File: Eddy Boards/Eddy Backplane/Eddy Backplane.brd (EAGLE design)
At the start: 154.2 x 120.7 mm, 87 parts, among them J1 USB_MINI-B_SMT, P1 39-30-02?_S, P2 RB1-125BAG1A, P3 39-30-04?_S, Q1 310mA/60V/1.6Ω, Q2 310mA/60V/1.6Ω, Q3 310mA/60V/1.6Ω, Q4 310mA/60V/1.6Ω, Q5 310mA/60V/1.6Ω, Q6 310mA/60V/1.6Ω, Q7 310mA/60V/1.6Ω, Q8 310mA/60V/1.6Ω, U1 W5500, U2 STM32F405RGT6, Y2 12MHz, Y3 32.768kHz

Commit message: Eddy backplane *mostly* complete. Just some minor things
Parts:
- moved SWITCH_CONN 88.1 mm to (151.8, 95.1), turned to 90 degrees
- moved U$8 82.3 mm to (144.4, 95.0), turned to 90 degrees
- moved PWR_ON 81.3 mm to (5.33, 95.9), turned to 90 degrees
- moved SWDIO/SWDCLK/RESET 80.5 mm to (76.3, 103.1), turned to 180 degrees
- moved S1 79.9 mm to (57.3, 116.2), turned to 180 degrees
- moved R20 76.0 mm to (67.6, 105.9)
- moved R21 76.0 mm to (67.6, 107.4)
- moved D5 75.9 mm to (72.8, 107.3)
- moved J1 75.9 mm to (71.4, 113.5)
- moved C24 71.4 mm to (63.1, 117.5), turned to 90 degrees
- moved R27 70.1 mm to (64.9, 117.5), turned to 270 degrees
- moved R30 64.0 mm to (78.7, 108.2)
- moved C20 63.8 mm to (82.8, 117.6), turned to 270 degrees
- moved R16 62.7 mm to (80.1, 111.6), turned to 270 degrees
- moved R9 62.1 mm to (121.8, 73.0), turned to 180 degrees
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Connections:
- removed net +3V3: C1.1, C2.1, C23.1, C24.1, C4.1, C5.1, C6.1, C7.1, P2.R3, Q1.1, Q2.1, Q3.1, Q4.1, Q5.1, Q6.1, Q7.1, Q8.1, R1.2, R2.1, R23.2, R25.1, R27.2, R28.1, R3.1, R31.1, R33.1, R35.1, R37.1, R39.1, R41.1, SWDIO/SWDCLK/RESET.1, SWDIO/SWDCLK/RESET.2, U1.11, U1.15, U1.17, U1.21, U1.28, U1.4, U1.8, U2.13, U2.19, U2.32, U2.48, U2.64
- net 3.3V: now also C1.1, C2.1, C23.1, C24.1, C4.1, C5.1, C6.1, C7.1, P2.R3, Q1.1, Q2.1, Q3.1, Q4.1, Q5.1, Q6.1, Q7.1, Q8.1, R1.2, R2.1, R23.2, R25.1, R27.2, R28.1, R3.1, R31.1, R33.1, R35.1, R37.1, R39.1, R41.1, SWDIO/SWDCLK/RESET.1, SWDIO/SWDCLK/RESET.2, U1.11, U1.15, U1.17, U1.21, U1.28, U1.4, U1.8, U2.13, U2.19, U2.32, U2.48, U2.64
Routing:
- net 3.3V: track 0.00 -> 457.6 mm, vias 0 -> 30
- net CONTROL_SIGNAL: track 97.2 -> 295.4 mm, vias 0 -> 4
- net SWITCH_3: track 168.8 -> 324.5 mm, vias 4 -> 1
- net 3.3V_ON/OFF: track 97.2 -> 241.6 mm, vias 0 -> 3
- net 5V_ON/OFF: track 97.2 -> 240.4 mm, vias 0 -> 3
- net SWITCH_4: track 184.3 -> 325.6 mm, vias 4 -> 1
- net SWITCH_2: track 176.3 -> 316.7 mm, vias 3 -> 1
- net 12V_ON/OFF: track 97.2 -> 230.0 mm, vias 0 -> 1
- net SWITCH_1: track 173.8 -> 305.4 mm, vias 3 -> 1
- net SWITCH_5: track 194.7 -> 325.7 mm, vias 2 -> 1
- net JETSON_ON/OFF: track 97.9 -> 214.7 mm, vias 0 -> 1
- net MOBO_ON/OFF: track 97.2 -> 212.4 mm, vias 0 -> 1
- net KILL_SWITCH: track 173.7 -> 288.3 mm, vias 2 -> 1
- net ROBOT_SDA: track 109.2 -> 219.6 mm
- net 5V: track 64.4 -> 157.6 mm, vias 0 -> 4
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- added copper zone on layer 1, net 3.3V
- added copper zone on layer 1, net 5V
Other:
- board text added: "Yo we could prob fit the battery balancer board on here too"
- board text removed: "How thick are our boards?"
- board text removed: "Questions to ask:"
- board text removed: "What size are the radii?"

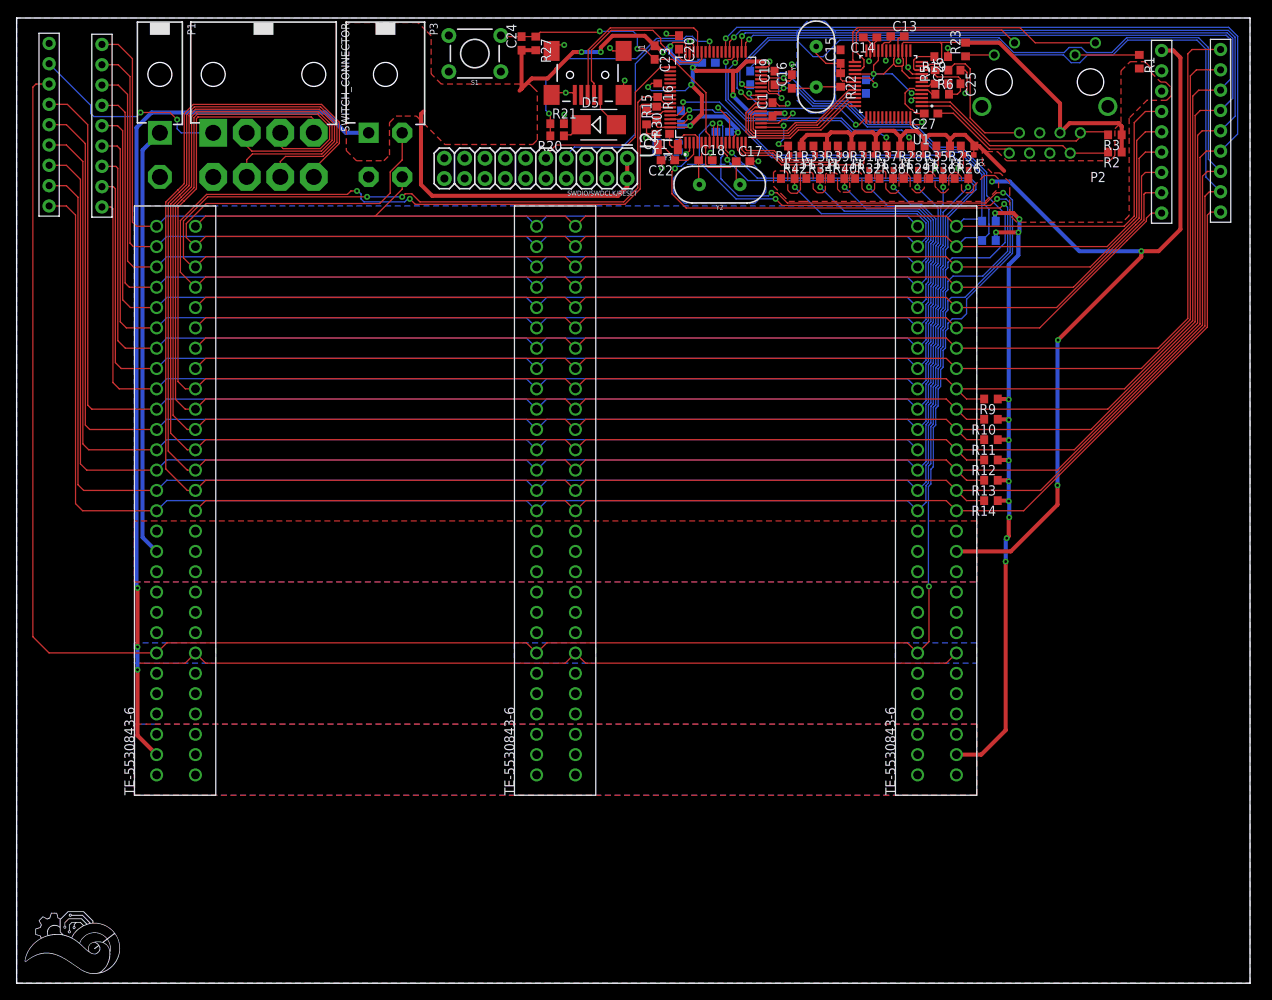
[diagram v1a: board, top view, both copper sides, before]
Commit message: Broken ground plane fixed. Ready for board review
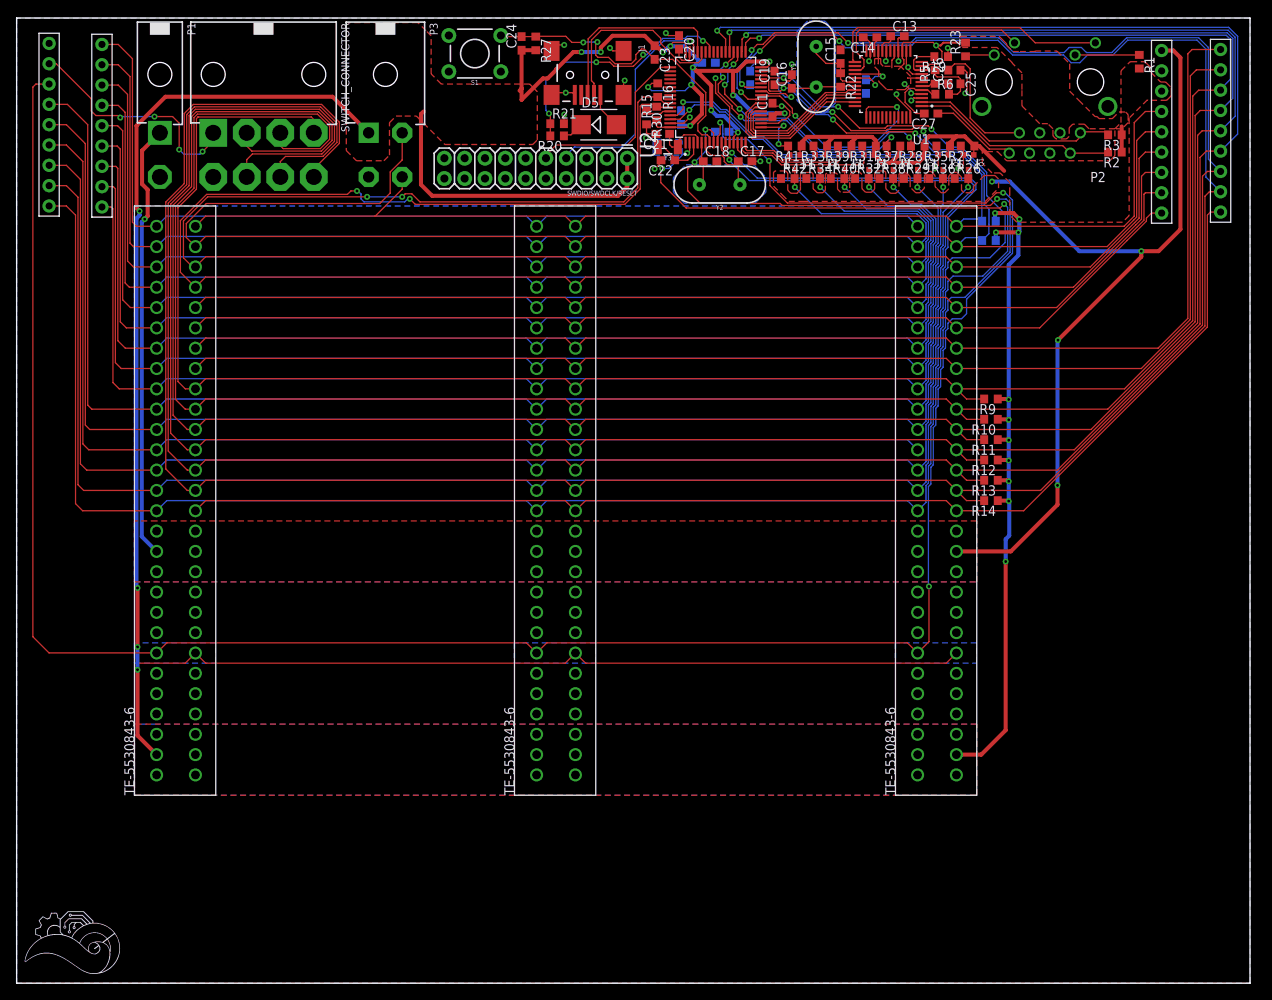
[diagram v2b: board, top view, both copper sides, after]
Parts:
- moved C18 0.59 mm to (86.7, 102.7)
- moved C17 0.25 mm to (91.1, 102.7)
- moved C1 0.06 mm to (94.5, 109.2)
- moved C7 0.06 mm to (88.2, 106.4)
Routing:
- net 3.3V: track 457.6 -> 429.2 mm, vias 30 -> 32
- net NET_RESET: track 18.4 -> 28.3 mm
- net GND: track 60.9 -> 66.5 mm, vias 24 -> 22
- net PLTA_ON/OFF: track 130.5 -> 134.6 mm, vias 2 -> 4
- net PWM_3V3_4: track 30.7 -> 34.1 mm, vias 2 -> 4
- net N$34: track 36.6 -> 39.4 mm
- net 3.3V_ON/OFF: track 241.6 -> 244.4 mm
- net 12V_ON/OFF: track 230.0 -> 232.2 mm, vias 1 -> 3
- net SWITCH_3: track 324.5 -> 326.6 mm
- net PWM_3V3_3: track 33.5 -> 35.6 mm, vias 2 -> 4
- net CONTROL_SIGNAL: track 295.4 -> 293.6 mm
- net 5V_ON/OFF: track 240.4 -> 242.0 mm
- net SWITCH_4: track 325.6 -> 327.0 mm, vias 1 -> 3
- net N$17: track 10.2 -> 9.18 mm
- net D+: track 23.2 -> 24.0 mm
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
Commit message: updated DRC error cleanup
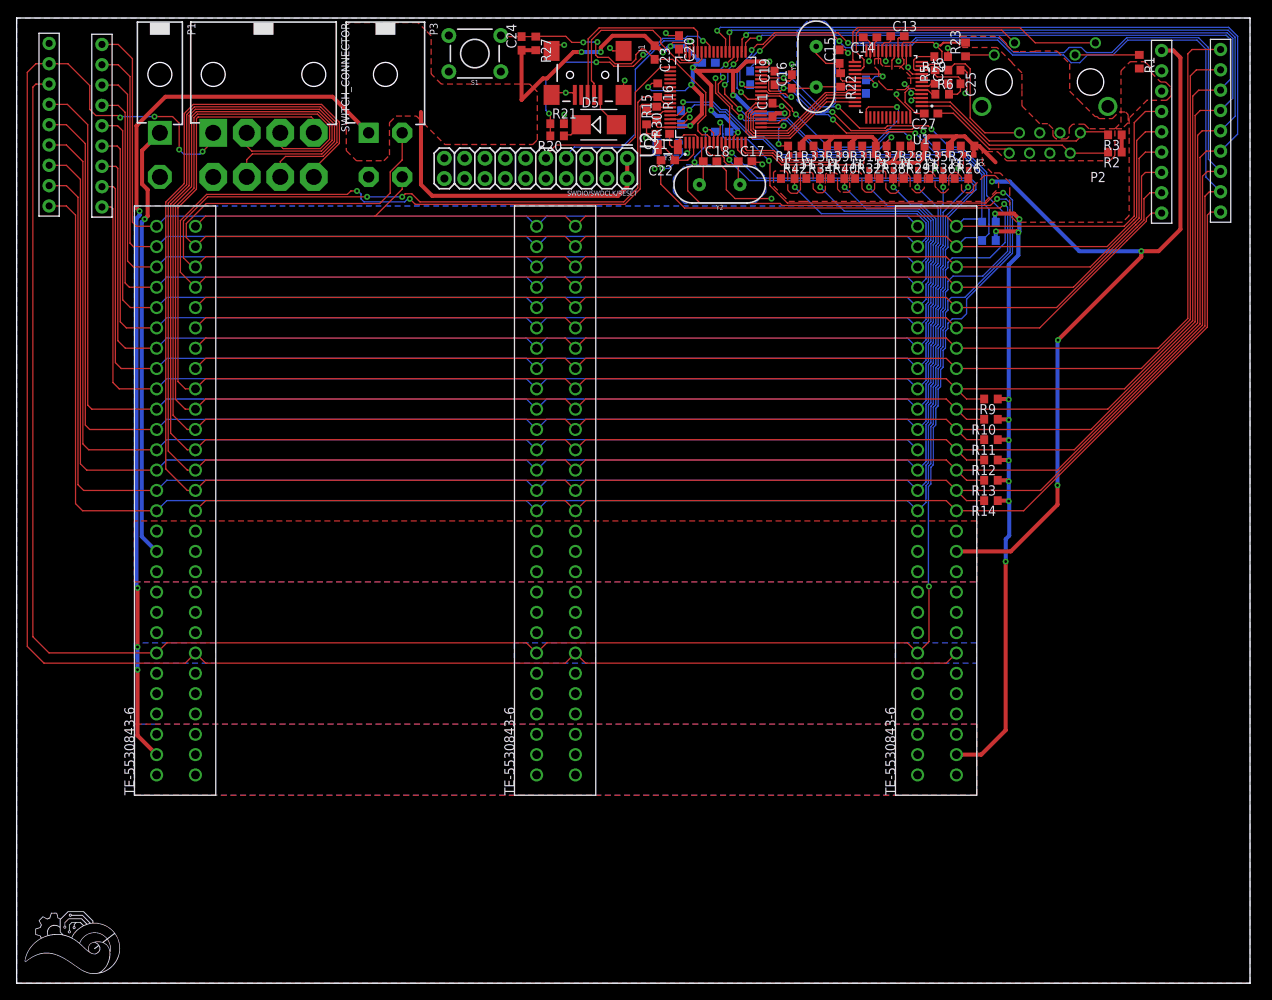
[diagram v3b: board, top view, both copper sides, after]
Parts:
- moved C15 0.13 mm to (102.9, 115.8)
- moved R18 0.13 mm to (121.5, 95.1)
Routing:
- net PLTA_ON/OFF: track 134.6 -> 225.3 mm
- net GND: track 66.5 -> 78.6 mm, vias 22 -> 24
- net 3.3V: track 429.2 -> 424.5 mm
- net N$30: track 4.12 -> 3.33 mm
- net VBUS: track 5.13 -> 4.55 mm
- net SWITCH_3: track 326.6 -> 326.0 mm
- removed copper zone on layer 1, net N$1
- removed copper zone on layer 1, net N$2

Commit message: Eddy Backplane Ready for board review round 1
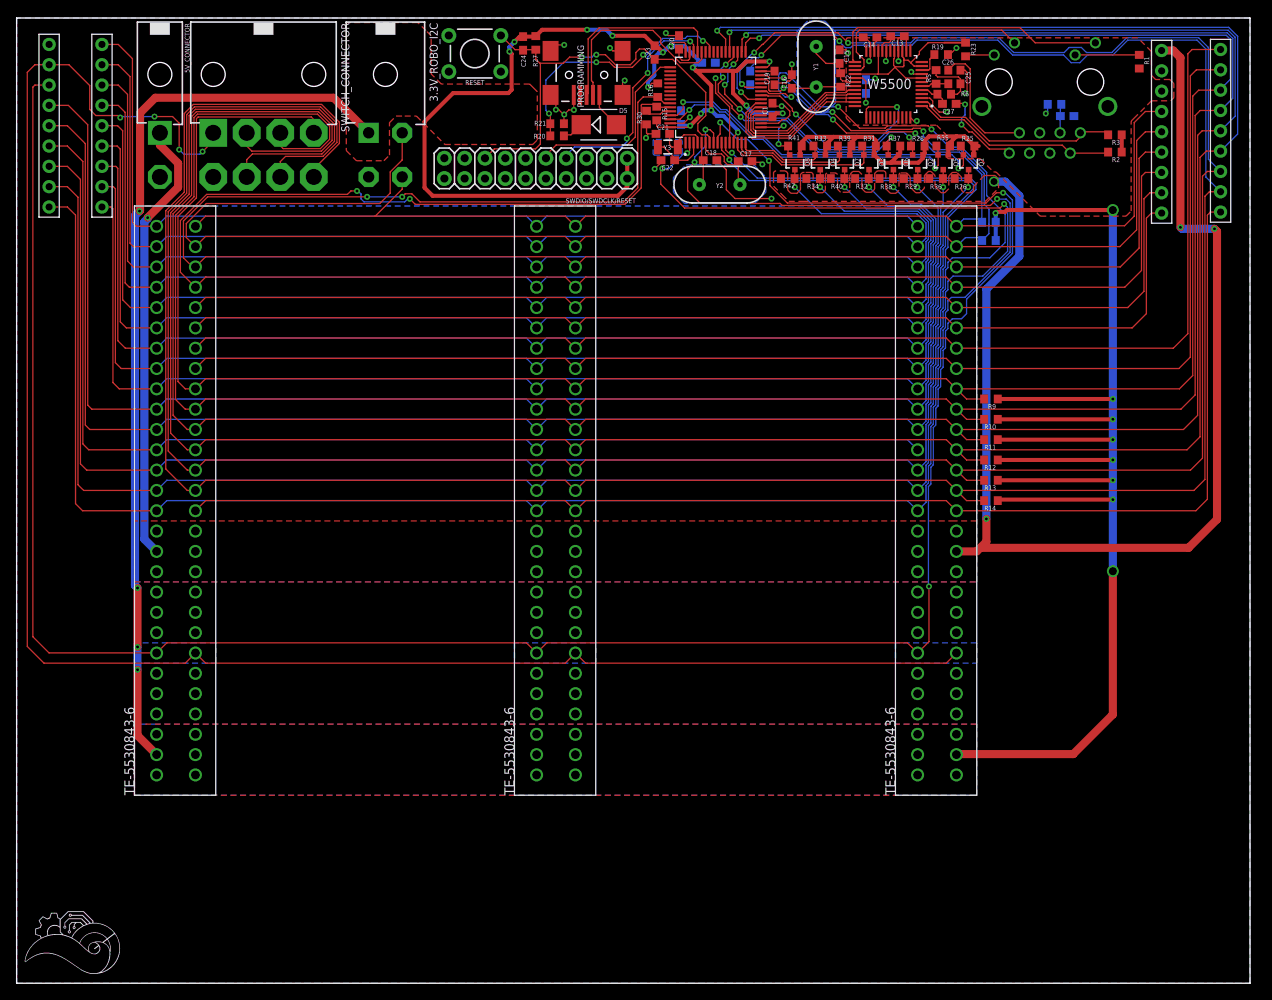
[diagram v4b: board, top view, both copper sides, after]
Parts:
- removed J1: USB_MINI-B_SMT, SparkFun-Connectors:USB-MINIB
- added PROGRAMMING: USB_MINI-B_SMT, SparkFun-Connectors:USB-MINIB
- added R4: 10, rcl:R0603
- C13: value (none) -> 4.7uF
- C14, C25: value (none) -> 10nF
- C15, C16: value (none) -> 18pF
- C26, C27: value (none) -> 6.8nF
- C7: value (none) -> 22nF
- R1, R23: value (none) -> 330
- R19: value (none) -> 12.4k
- R2, R3: value (none) -> 49
- R22: value (none) -> 1M
- R5, R6: value (none) -> 82
- Y1: value (none) -> 25Mhz
- moved C7 43.2 mm to (131.3, 108.4), turned to 180 degrees
- moved C27 2.58 mm to (116.6, 109.9)
- moved R19 0.25 mm to (115.6, 116.1)
- moved R6 0.25 mm to (116.0, 111.1)
- moved C24 0.19 mm to (63.3, 117.5), turned to 270 degrees
- moved C18 0.13 mm to (86.7, 102.9)
- moved PWR_ON 0.13 mm to (5.33, 95.8)
- moved R5 0.13 mm to (114.9, 113.3)
- moved R27 0.06 mm to (64.9, 117.5), turned to 90 degrees
- renumbered P1 to 5V_CONNECTOR, P3 to 3.3V_ROBO_I2C, S1 to RESET, U1 to W5500, U2 to STM32
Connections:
- removed net N$34: C23.2, C24.2, R27.1, RESET.3, STM32.7
- new net N$1: C7.1, P2.R3, R4.2
- new net RESET: C23.2, C24.2, R27.1, RESET.3, STM32.7, SWDIO/SWDCLK/RESET.15
- net 3.3V: now also R4.1; no longer C7.1, P2.R3
- net D+: now also PROGRAMMING.D+; no longer J1.D+
- net D-: now also PROGRAMMING.D-; no longer J1.D-
- net GND: now also PROGRAMMING.GND, PROGRAMMING.S1, PROGRAMMING.S2, PROGRAMMING.S3, PROGRAMMING.S4; no longer J1.GND, J1.S1, J1.S2, J1.S3, J1.S4
- net VBUS: now also PROGRAMMING.VBUS; no longer J1.VBUS
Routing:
- net 3.3V: track 424.5 -> 521.9 mm, vias 32 -> 30
- net RESET: track 0.00 -> 57.8 mm, vias 0 -> 2
- net 5V: track 158.2 -> 204.5 mm
- net N$34: track 39.4 -> 0.00 mm, vias 2 -> 0
- net SPARE7: track 153.9 -> 166.5 mm
- net SWITCH_5: track 325.4 -> 336.5 mm
- net SWITCH_4: track 327.0 -> 336.4 mm
- net SWITCH_3: track 326.0 -> 334.3 mm
- net SWITCH_2: track 317.4 -> 324.2 mm
- net SPARE4: track 129.0 -> 135.8 mm
- net SWITCH_1: track 305.0 -> 310.4 mm
- net SPARE3: track 130.4 -> 135.6 mm
- net N$27: track 8.50 -> 3.64 mm
- net KILL_SWITCH: track 288.3 -> 292.3 mm
- net GND: track 78.6 -> 82.4 mm, vias 24 -> 25
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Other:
- board text added: "12V On/Off"
- board text added: "3.3V"
- board text added: "3.3V On/Off"
- board text added: "5V"
- board text added: "5V On/Off"
- board text added: "Acoustic On/Off"
- board text added: "Control Signal"
- board text added: "GND"
- board text added: "Jestson On/Off"
- board text added: "Kill Switch"
- board text added: "Mobo On/Off"
- board text added: "PLTA On/Off"
- board text added: "PWM 1"
- board text added: "PWM 2"
- board text added: "PWM 3"
- board text added: "PWM 4"
- board text added: "PWM 5"
- board text added: "PWM 6"
- board text added: "PWM 7"
- board text added: "PWM 8"
- board text added: "Robot SCL"
- board text added: "Robot SDA"
- board text added: "SWCLK"
- board text added: "SWDIO"
- board text added: "Spare 2"
- board text added: "Switch 1"
- board text added: "Switch 2"
- board text added: "Switch 3"
- board text added: "Switch 4"
- board text added: "Switch 5"
- board text removed: "Yo we could prob fit the battery balancer board on here too"

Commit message: update with board review changed
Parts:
- moved R2 4.77 mm to (133.0, 101.7), turned to 90 degrees
- moved R3 3.59 mm to (134.4, 103.9), turned to 90 degrees
- moved R23 2.26 mm to (120.0, 114.9)
- moved R1 1.91 mm to (138.4, 115.3)
- moved C16 0.14 mm to (97.0, 112.8)
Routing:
- net 3.3V: track 521.9 -> 531.5 mm
- net PWM_3V3_8: track 8.09 -> 11.9 mm
- net N$24: track 25.8 -> 22.8 mm
- net GND: track 82.4 -> 79.7 mm
- net N$16: track 8.03 -> 6.15 mm
- net N$23: track 26.4 -> 24.9 mm
- net CONTROL_SIGNAL: track 292.7 -> 291.4 mm
- net N$28: track 11.4 -> 12.2 mm
- net N$15: track 3.65 -> 3.15 mm
